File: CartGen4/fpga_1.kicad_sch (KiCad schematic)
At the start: 5 parts, among them U9 LFXP2-8E-5MN132C

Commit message: Updated field information
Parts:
- C36, C37, C38, C39: Package ID (none) -> 0402
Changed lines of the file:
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@@
+      (effects (font (size 1.27 1.27)) hide)
+    )
+    (property "Description" "~" (id 7) (at 238.76 133.35 0)
+      (effects (font (size 1.27 1.27)) hide)
+    )
+    (property "MFN" "~" (id 8) (at 238.76 133.35 0)
+      (effects (font (size 1.27 1.27)) hide)
+    )
+    (property "MFP" "~" (id 9) (at 238.76 133.35 0)
+      (effects (font (size 1.27 1.27)) hide)
+    )
+    (property "Package ID" "0402" (id 10) (at 238.76 133.35 0)
       (effects (font (size 1.27 1.27)) hide)
     )
@@
       (effects (font (size 1.27 1.27)) hide)
     )
+    (property "Description" "~" (id 7) (at 251.46 133.35 0)
+      (effects (font (size 1.27 1.27)) hide)
+    )
+    (property "MFN" "~" (id 8) (at 251.46 133.35 0)
+      (effects (font (size 1.27 1.27)) hide)
+    )
+    (property "MFP" "~" (id 9) (at 251.46 133.35 0)
+      (effects (font (size 1.27 1.27)) hide)
+    )
+    (property "Package ID" "0402" (id 10) (at 251.46 133.35 0)
+      (effects (font (size 1.27 1.27)) hide)
+    )
     (pin "1")
     (pin "2")
@@
       (effects (font (size 1.27 1.27)) hide)
     )
+    (property "Description" "~" (id 7) (at 213.36 133.35 0)
+      (effects (font (size 1.27 1.27)) hide)
+    )
+    (property "MFN" "~" (id 8) (at 213.36 133.35 0)
+      (effects (font (size 1.27 1.27)) hide)
+    )
+    (property "MFP" "~" (id 9) (at 213.36 133.35 0)
+      (effects (font (size 1.27 1.27)) hide)
+    )
+    (property "Package ID" "0402" (id 10) (at 213.36 133.35 0)
+      (effects (font (size 1.27 1.27)) hide)
+    )
     (pin "1")
     (pin "2")
@@
       (effects (font (size 1.27 1.27)) hide)
     )
+    (property "Description" "~" (id 7) (at 226.06 133.35 0)
+      (effects (font (size 1.27 1.27)) hide)
+    )
+    (property "MFN" "~" (id 8) (at 226.06 133.35 0)
+      (effects (font (size 1.27 1.27)) hide)
+    )
+    (property "MFP" "~" (id 9) (at 226.06 133.35 0)
+      (effects (font (size 1.27 1.27)) hide)
+    )
+    (property "Package ID" "0402" (id 10) (at 226.06 133.35 0)
+      (effects (font (size 1.27 1.27)) hide)
+    )

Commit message: Updated some component fields
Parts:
- C36, C37, C38, C39: Supplier suggestion (none) -> https://nl.mouser.com/ProductDetail/Murata-Electronics/GRM1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; Tolerance (none) -> 20%; Voltage (none) -> 3V3
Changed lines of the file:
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@@
+      (effects (font (size 1.27 1.27)) hide)
+    )
+    (property "Supplier suggestion" "https://nl.mouser.com/ProductDetail/Murata-Electronics/GRM155R61C104KA88J?qs=sGAEpiMZZMsh%252B1woXyUXj8YF%2FGivH5Kx4uStnYyl8jU%3D" (id 11) (at 238.76 133.35 0)
+      (effects (font (size 1.27 1.27)) hide)
+    )
+    (property "Tolerance" "20%" (id 12) (at 238.76 133.35 0)
+      (effects (font (size 1.27 1.27)) hide)
+    )
+    (property "Voltage" "3V3" (id 13) (at 238.76 133.35 0)
       (effects (font (size 1.27 1.27)) hide)
     )
@@
       (effects (font (size 1.27 1.27)) hide)
     )
+    (property "Supplier suggestion" "https://nl.mouser.com/ProductDetail/Murata-Electronics/GRM155R61C104KA88J?qs=sGAEpiMZZMsh%252B1woXyUXj8YF%2FGivH5Kx4uStnYyl8jU%3D" (id 11) (at 251.46 133.35 0)
+      (effects (font (size 1.27 1.27)) hide)
+    )
+    (property "Tolerance" "20%" (id 12) (at 251.46 133.35 0)
+      (effects (font (size 1.27 1.27)) hide)
+    )
+    (property "Voltage" "3V3" (id 13) (at 251.46 133.35 0)
+      (effects (font (size 1.27 1.27)) hide)
+    )
     (pin "1")
     (pin "2")
@@
       (effects (font (size 1.27 1.27)) hide)
     )
+    (property "Supplier suggestion" "https://nl.mouser.com/ProductDetail/Murata-Electronics/GRM155R61C104KA88J?qs=sGAEpiMZZMsh%252B1woXyUXj8YF%2FGivH5Kx4uStnYyl8jU%3D" (id 11) (at 213.36 133.35 0)
+      (effects (font (size 1.27 1.27)) hide)
+    )
+    (property "Tolerance" "20%" (id 12) (at 213.36 133.35 0)
+      (effects (font (size 1.27 1.27)) hide)
+    )
+    (property "Voltage" "3V3" (id 13) (at 213.36 133.35 0)
+      (effects (font (size 1.27 1.27)) hide)
+    )
     (pin "1")
     (pin "2")
@@
       (effects (font (size 1.27 1.27)) hide)
     )
+    (property "Supplier suggestion" "https://nl.mouser.com/ProductDetail/Murata-Electronics/GRM155R61C104KA88J?qs=sGAEpiMZZMsh%252B1woXyUXj8YF%2FGivH5Kx4uStnYyl8jU%3D" (id 11) (at 226.06 133.35 0)
+      (effects (font (size 1.27 1.27)) hide)
+    )
+    (property "Tolerance" "20%" (id 12) (at 226.06 133.35 0)
+      (effects (font (size 1.27 1.27)) hide)
+    )
+    (property "Voltage" "3V3" (id 13) (at 226.06 133.35 0)
+      (effects (font (size 1.27 1.27)) hide)
+    )

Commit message: Added missing recommendations
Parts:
- U9: Supplier suggestion (none) -> https://nl.mouser.com/ProductDetail/Lattice/LFXP2-8E-5MN132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
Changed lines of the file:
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@@
+      (effects (font (size 1.27 1.27)) hide)
+    )
+    (property "Supplier suggestion" "https://nl.mouser.com/ProductDetail/Lattice/LFXP2-8E-5MN132C?qs=8xMK%252BwDsXhfJ8B0GIKbr4g%3D%3D" (id 11) (at 55.88 140.97 0)
       (effects (font (size 1.27 1.27)) hide)
     )
@@
       (effects (font (size 1.27 1.27)) hide)
     )
+    (property "Supplier suggestion" "https://nl.mouser.com/ProductDetail/Lattice/LFXP2-8E-5MN132C?qs=8xMK%252BwDsXhfJ8B0GIKbr4g%3D%3D" (id 11) (at 133.35 140.97 0)
+      (effects (font (size 1.27 1.27)) hide)
+    )
     (pin "A11")
     (pin "A12")
@@
     )
     (property "Source" "SPEC" (id 10) (at 66.04 53.34 0)
+      (effects (font (size 1.27 1.27)) hide)
+    )
+    (property "Supplier suggestion" "https://nl.mouser.com/ProductDetail/Lattice/LFXP2-8E-5MN132C?qs=8xMK%252BwDsXhfJ8B0GIKbr4g%3D%3D" (id 11) (at 66.04 53.34 0)
       (effects (font (size 1.27 1.27)) hide)
     )
@@
     )
     (property "Source" "SPEC" (id 10) (at 144.78 57.15 0)
+      (effects (font (size 1.27 1.27)) hide)
+    )
+    (property "Supplier suggestion" "https://nl.mouser.com/ProductDetail/Lattice/LFXP2-8E-5MN132C?qs=8xMK%252BwDsXhfJ8B0GIKbr4g%3D%3D" (id 11) (at 144.78 57.15 0)
       (effects (font (size 1.27 1.27)) hide)
     )
@@
       (effects (font (size 1.27 1.27)) hide)
     )
+    (property "Supplier suggestion" "https://nl.mouser.com/ProductDetail/Lattice/LFXP2-8E-5MN132C?qs=8xMK%252BwDsXhfJ8B0GIKbr4g%3D%3D" (id 11) (at 228.6 49.53 0)
+      (effects (font (size 1.27 1.27)) hide)
+    )

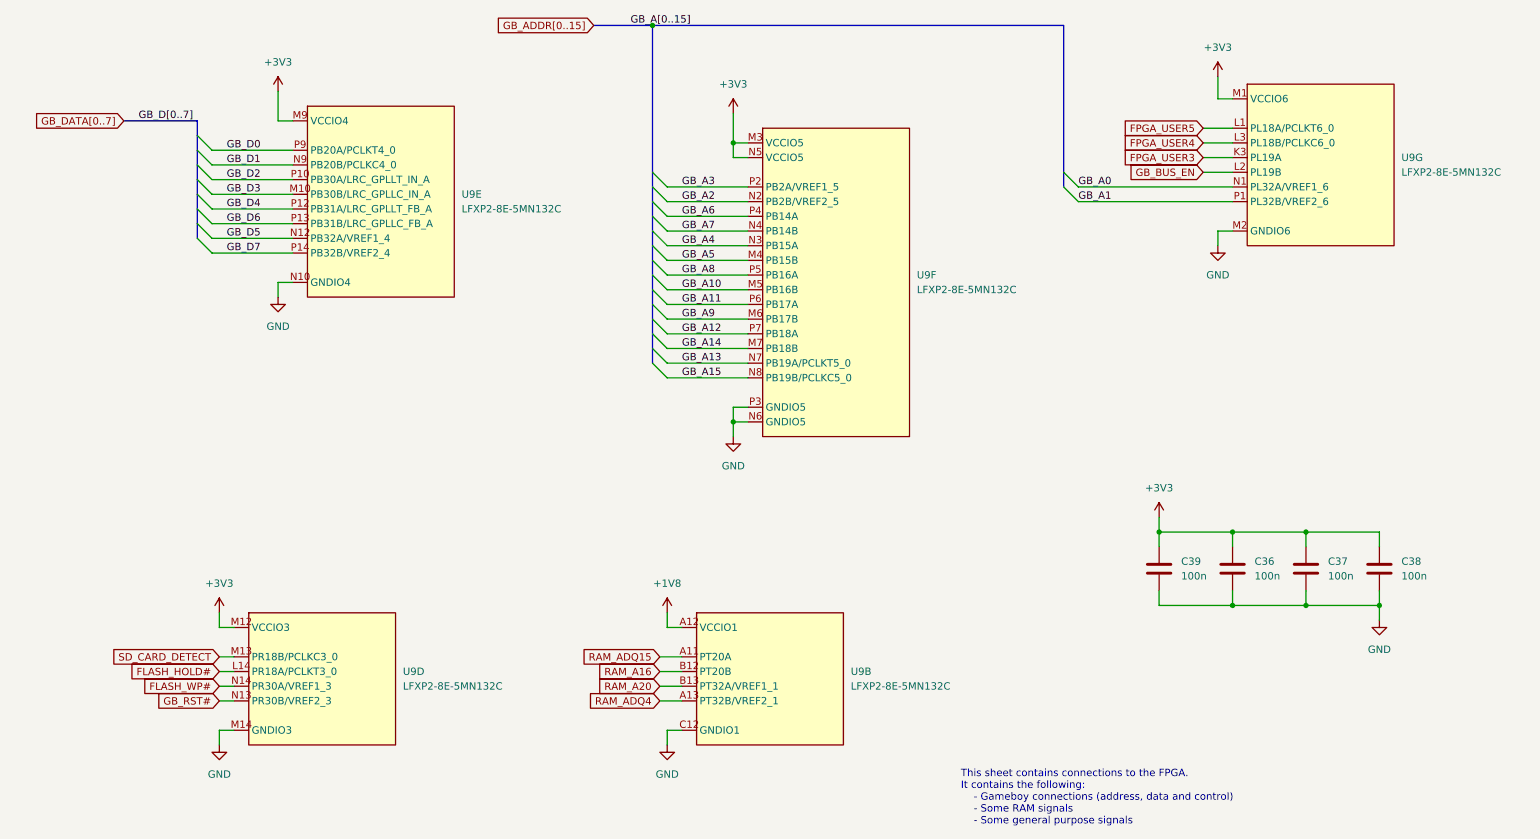
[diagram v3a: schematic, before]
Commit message: Reassigned RD geographically
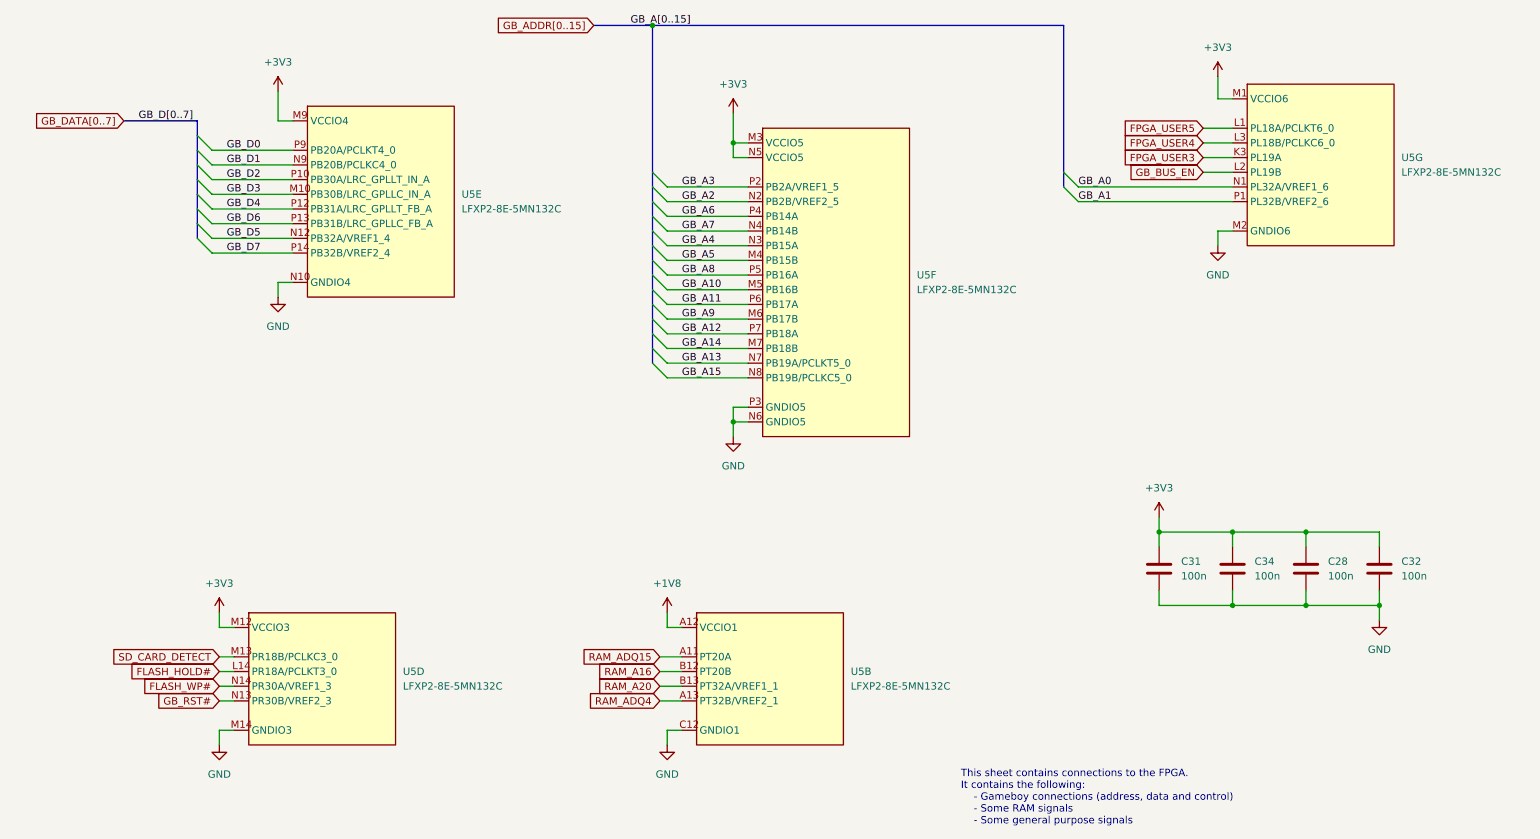
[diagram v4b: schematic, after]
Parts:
- renumbered C37 to C28, C39 to C31, C38 to C32, C36 to C34, U9 to U5
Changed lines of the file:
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@@
   (symbol (lib_id "Device:C") (at 238.76 133.35 0) (unit 1)
     (in_bom yes) (on_board yes) (fields_autoplaced)
-    (property "Reference" "C37" (id 0) (at 242.57 132.0799 0)
+    (property "Reference" "C28" (id 0) (at 242.57 132.0799 0)
       (effects (font (size 1.27 1.27)) (justify left))
     )
@@
   (symbol (lib_id "FPGA_Lattice:LFXP2-8E-5MN132C") (at 55.88 140.97 0) (unit 4)
     (in_bom yes) (on_board yes) (fields_autoplaced)
-    (property "Reference" "U9" (id 0) (at 82.55 151.1299 0)
+    (property "Reference" "U5" (id 0) (at 82.55 151.1299 0)
       (effects (font (size 1.27 1.27)) (justify left))
     )
@@
   (symbol (lib_id "FPGA_Lattice:LFXP2-8E-5MN132C") (at 133.35 140.97 0) (unit 2)
     (in_bom yes) (on_board yes) (fields_autoplaced)
-    (property "Reference" "U9" (id 0) (at 160.02 151.1299 0)
+    (property "Reference" "U5" (id 0) (at 160.02 151.1299 0)
       (effects (font (size 1.27 1.27)) (justify left))
     )
@@
   (symbol (lib_id "Device:C") (at 251.46 133.35 0) (unit 1)
     (in_bom yes) (on_board yes) (fields_autoplaced)
-    (property "Reference" "C38" (id 0) (at 255.27 132.0799 0)
+    (property "Reference" "C32" (id 0) (at 255.27 132.0799 0)
       (effects (font (size 1.27 1.27)) (justify left))
     )
@@
   (symbol (lib_id "Device:C") (at 213.36 133.35 0) (unit 1)
     (in_bom yes) (on_board yes) (fields_autoplaced)
-    (property "Reference" "C39" (id 0) (at 217.17 132.0799 0)
+    (property "Reference" "C31" (id 0) (at 217.17 132.0799 0)
       (effects (font (size 1.27 1.27)) (justify left))
     )
@@
   (symbol (lib_id "Device:C") (at 226.06 133.35 0) (unit 1)
     (in_bom yes) (on_board yes) (fields_autoplaced)
-    (property "Reference" "C36" (id 0) (at 229.87 132.0799 0)
+    (property "Reference" "C34" (id 0) (at 229.87 132.0799 0)
       (effects (font (size 1.27 1.27)) (justify left))
     )
@@
   (symbol (lib_id "FPGA_Lattice:LFXP2-8E-5MN132C") (at 66.04 53.34 0) (unit 5)
     (in_bom yes) (on_board yes) (fields_autoplaced)
-    (property "Reference" "U9" (id 0) (at 92.71 68.5799 0)
+    (property "Reference" "U5" (id 0) (at 92.71 68.5799 0)
       (effects (font (size 1.27 1.27)) (justify left))
     )
@@
   (symbol (lib_id "FPGA_Lattice:LFXP2-8E-5MN132C") (at 144.78 57.15 0) (unit 6)
     (in_bom yes) (on_board yes) (fields_autoplaced)
-    (property "Reference" "U9" (id 0) (at 171.45 82.5499 0)
+    (property "Reference" "U5" (id 0) (at 171.45 82.5499 0)
       (effects (font (size 1.27 1.27)) (justify left))
     )
@@
   (symbol (lib_id "FPGA_Lattice:LFXP2-8E-5MN132C") (at 228.6 49.53 0) (unit 7)
     (in_bom yes) (on_board yes) (fields_autoplaced)
-    (property "Reference" "U9" (id 0) (at 255.27 62.2299 0)
-      (effects (font (size 1.27 1.27)) (justify left))
-    )
+    (property "Reference" "U5" (id 0) (at 255.27 62.2299 0)
+      (effects (font (size 1.27 1.27)) (justify left))
+    )
